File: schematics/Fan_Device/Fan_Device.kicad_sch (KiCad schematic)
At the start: 14 parts, among them J2 Barrel_Jack_Switch, SW1 SW_Push_Dual, SW4 SW_Push_Dual, U1 ESP32S-WROOM-32, U2 LM2596 Step Down

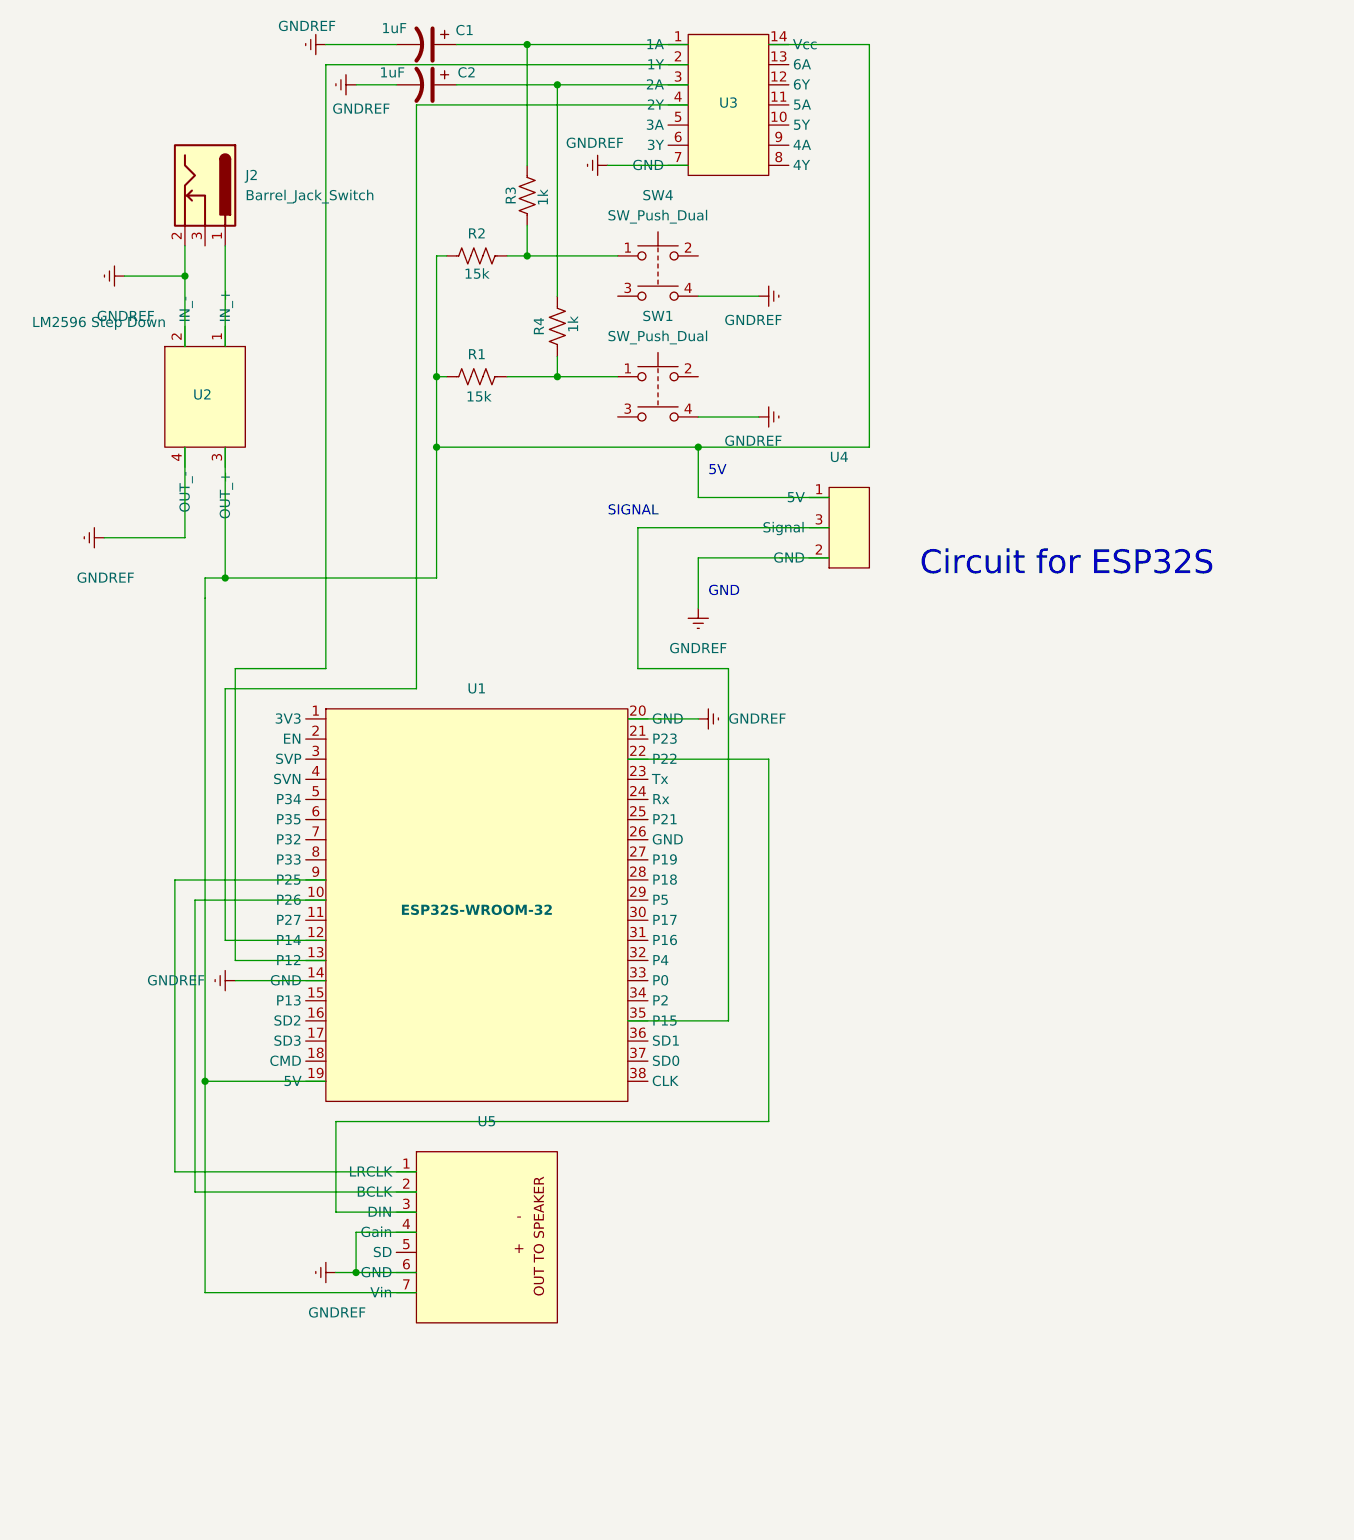
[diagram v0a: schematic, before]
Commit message: Reorganization of Hardware Files
Reorganized hardware schematics, symbols, and footprints for easy navigation
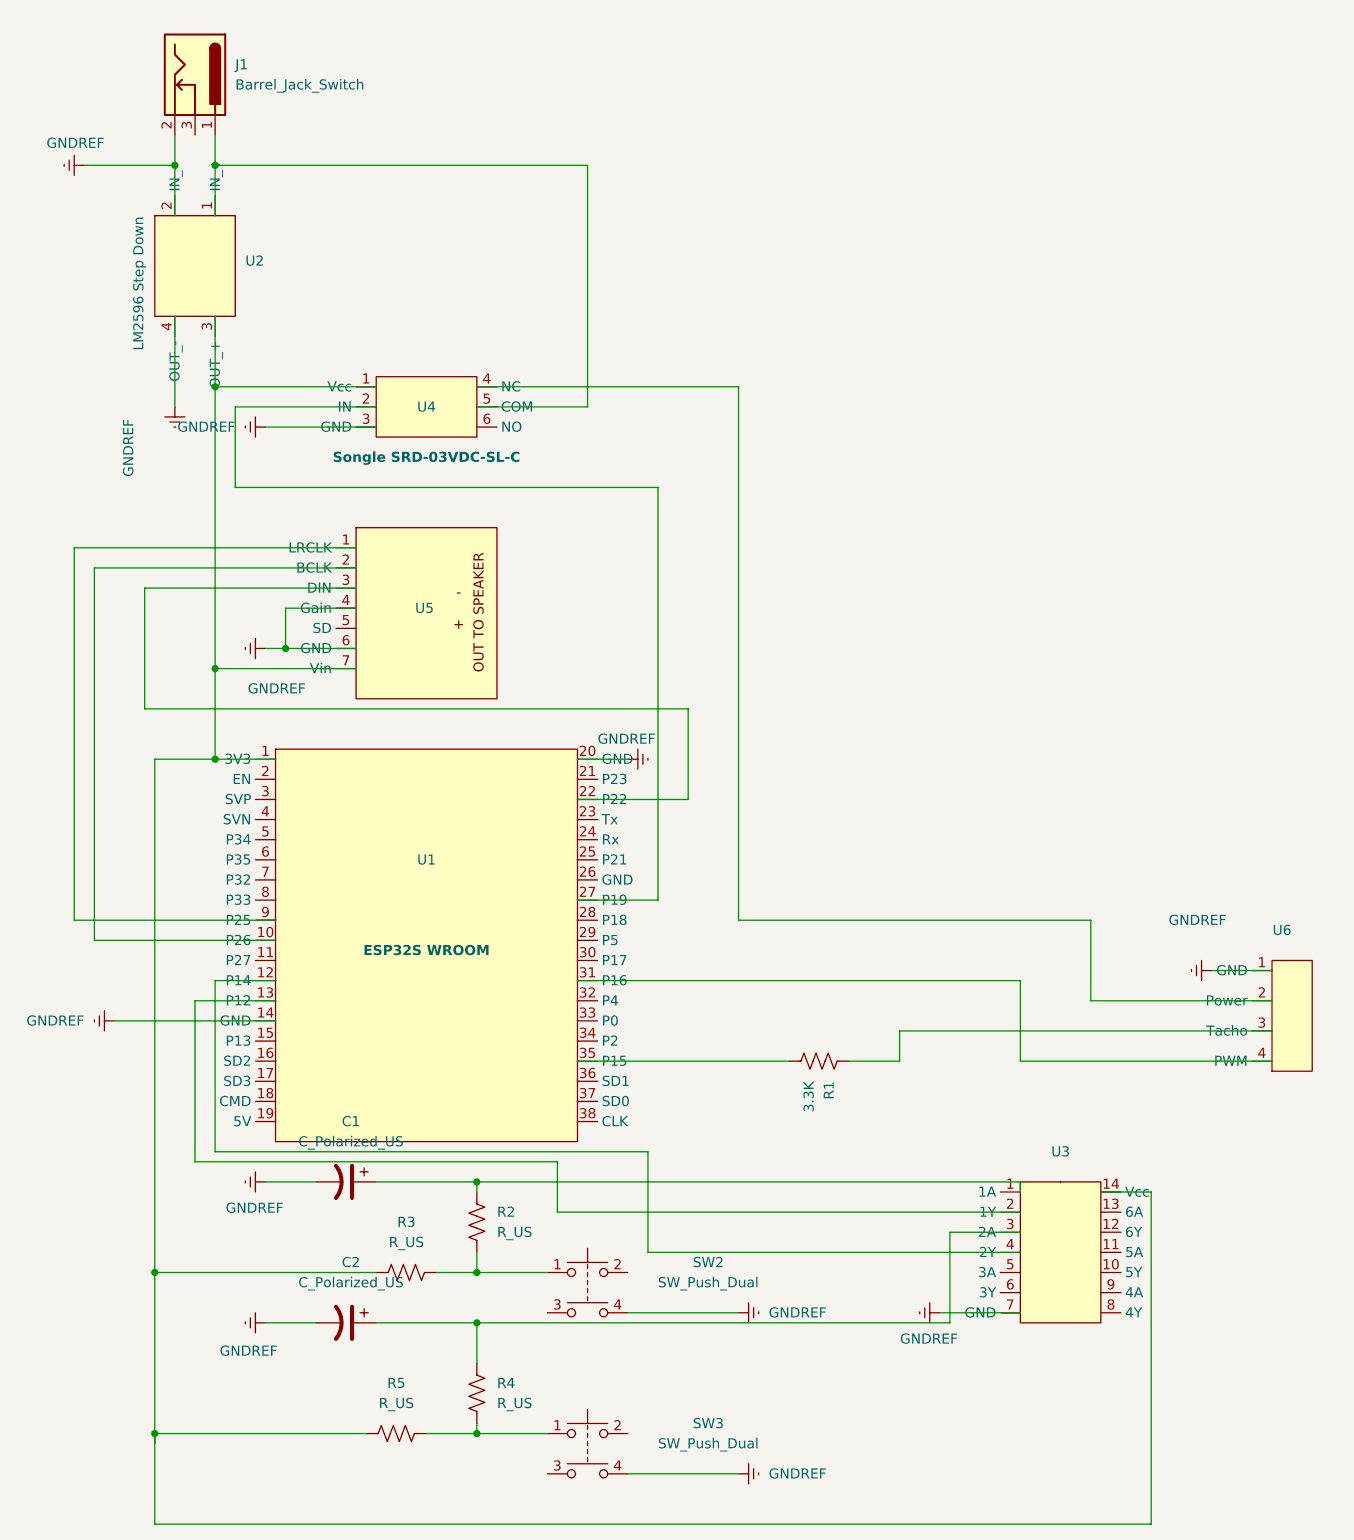
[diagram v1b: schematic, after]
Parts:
- removed J2: Barrel_Jack_Switch, CustomConnector:BarrelJack_Kycon_KLDX-0202-xC_Horizontal (BreadBoard), symbol Connector:Barrel_Jack_Switch
- removed SW1, SW4: SW_Push_Dual, Button_Switch_THT:SW_PUSH_6mm_H5mm, symbol Switch:SW_Push_Dual
- removed U4: ~, CustomConnector:MountingRail3x1, symbol 1A_CustomSymbols:LED_Connector
- added J1: Barrel_Jack_Switch, CustomConnector:BarrelJack_Kycon_KLDX-0202-xC_Horizontal (BreadBoard), symbol Connector:Barrel_Jack_Switch
- added R5: R_US, Resistor_THT:R_Axial_DIN0309_L9.0mm_D3.2mm_P15.24mm_Horizontal, symbol Device:R_US
- added SW2, SW3: SW_Push_Dual, Button_Switch_THT:SW_PUSH_6mm_H5mm, symbol Switch:SW_Push_Dual
- added U4: Songle SRD-03VDC-SL-C, Songle:Songle Relay Module, symbol 1A-Power:Songle
- added U6: ~, Connector_PinHeader_2.54mm:PinHeader_1x04_P2.54mm_Vertical, symbol 1A_CustomSymbols:Fan_Connector
- C1, C2: value 1uF -> C_Polarized_US
- R1: value 15k -> 3.3K
- R2: value 15k -> R_US
- R3, R4: value 1k -> R_US
- U1: value ESP32S-WROOM-32 -> ESP32S WROOM
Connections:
- net GNDREF: now also J1.2, SW2.4, SW3.4, U4.3 (GND), U6.1 (GND)
- net at U2.3 (OUT_+), U3.14 (Vcc), U5.7 (Vin): now also R3.2, U1.1 (3V3), R5.2, U4.1 (Vcc); no longer R1.1, R2.1, U1.19 (5V)
- net at R2.2, R3.1: now also SW2.1
- net at U1.27 (P19): now also U4.2 (IN)
- net at U1.31 (P16): now also U6.4 (PWM)
- net at U1.35 (P15): now also R1.2
- net at R4.1: now also C2.1, U3.3 (2A); no longer R1.2
- net at U2.1 (IN_+): now also J1.1, U4.5 (COM)
- net at C1.1, U3.1 (1A): now also R2.1; no longer R3.2
- new net: R4.2, R5.1, SW3.1
- new net: U4.4 (NC), U6.2 (Power)
- new net: R1.1, U6.3 (Tacho)
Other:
- note removed: "5V"
- note removed: "Circuit for ESP32S"
- note removed: "GND"
- note removed: "SIGNAL"
- title: ESP32S Based LED Controller -> Fan Control Device
